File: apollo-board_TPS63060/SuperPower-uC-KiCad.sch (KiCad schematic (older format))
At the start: 5 parts, among them J10 Conn_01x13_Male

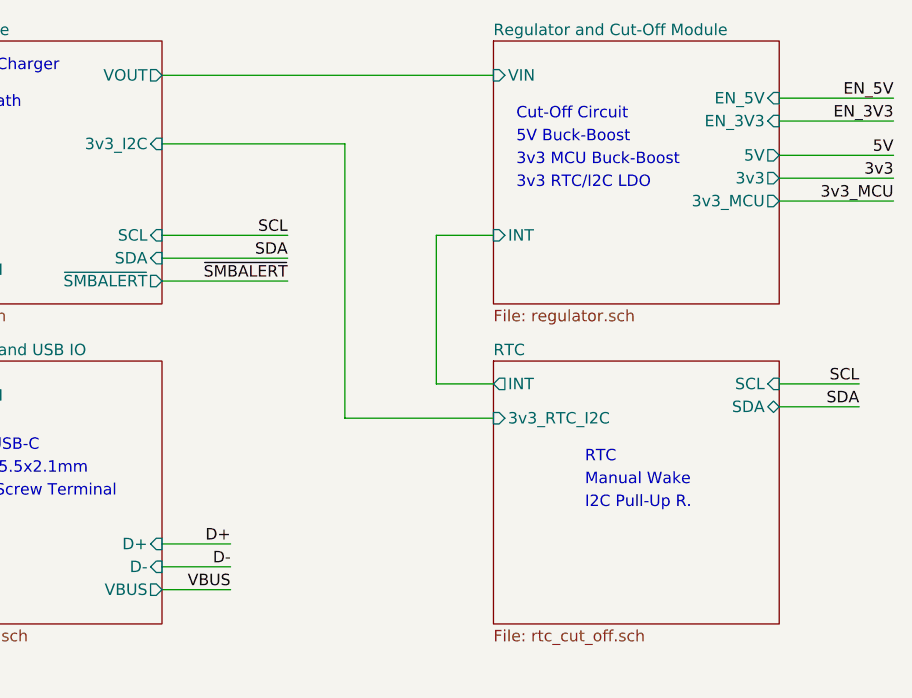
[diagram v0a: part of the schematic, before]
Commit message: Recreate TPS709 symbol to and set footprint to SOT23-5
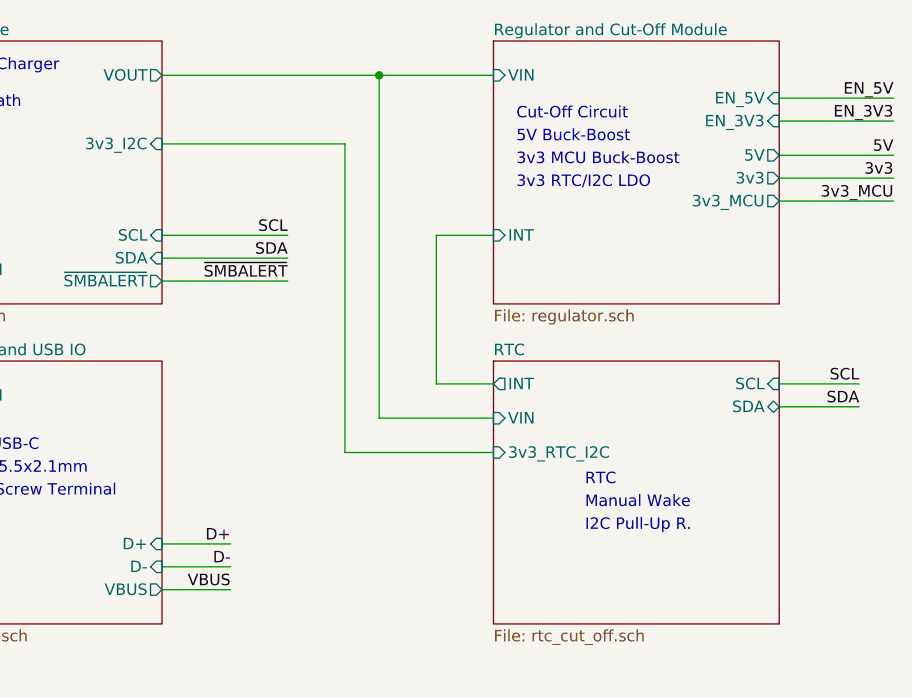
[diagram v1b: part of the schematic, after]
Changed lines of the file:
@@
 Text Notes 5850 2550 0    50   ~ 0
 5V Buck-Boost
-Text Notes 6150 3950 0    50   ~ 0
+Text Notes 6150 4050 0    50   ~ 0
 RTC
 Text Notes 5850 2450 0    50   ~ 0
@@
 Text Notes 3100 4100 0    50   ~ 0
 Solder Pads / Screw Terminal
-Text Notes 6150 4050 0    50   ~ 0
+Text Notes 6150 4150 0    50   ~ 0
 Manual Wake
 $Sheet
@@
 F2 "SCL" I R 7000 3600 50
 F3 "SDA" B R 7000 3700 50
-F4 "3v3_RTC_I2C" I L 5750 3750 50
+F4 "3v3_RTC_I2C" I L 5750 3900 50
 F5 "INT" O L 5750 3600 50
+F6 "VIN" I L 5750 3750 50
 $EndSheet
 Wire Wire Line
 	2950 3100 2950 3650
 Wire Wire Line
-	5750 2250 4300 2250
+	5750 2250 5250 2250
 Text Label 4850 2950 2    50   ~ 0
 SCL
@@
 F8 "INT" I L 5750 2950 50
 $EndSheet
-Text Notes 6150 4150 0    50   ~ 0
+Text Notes 6150 4250 0    50   ~ 0
 I2C Pull-Up R.
 Wire Wire Line
 	5100 2550 4300 2550
-Wire Wire Line
-	5750 3750 5100 3750
-Wire Wire Line
-	5100 2550 5100 3750
 Wire Wire Line
 	5500 3600 5500 2950
@@
 Wire Notes Line
 	1300 5350 2550 5350
+Wire Wire Line
+	5750 3900 5100 3900
+Wire Wire Line
+	5100 2550 5100 3900
+Wire Wire Line
+	5750 3750 5250 3750
+Wire Wire Line
+	5250 3750 5250 2250
+Connection ~ 5250 2250
+Wire Wire Line
+	5250 2250 4300 2250
 $EndSCHEMATC

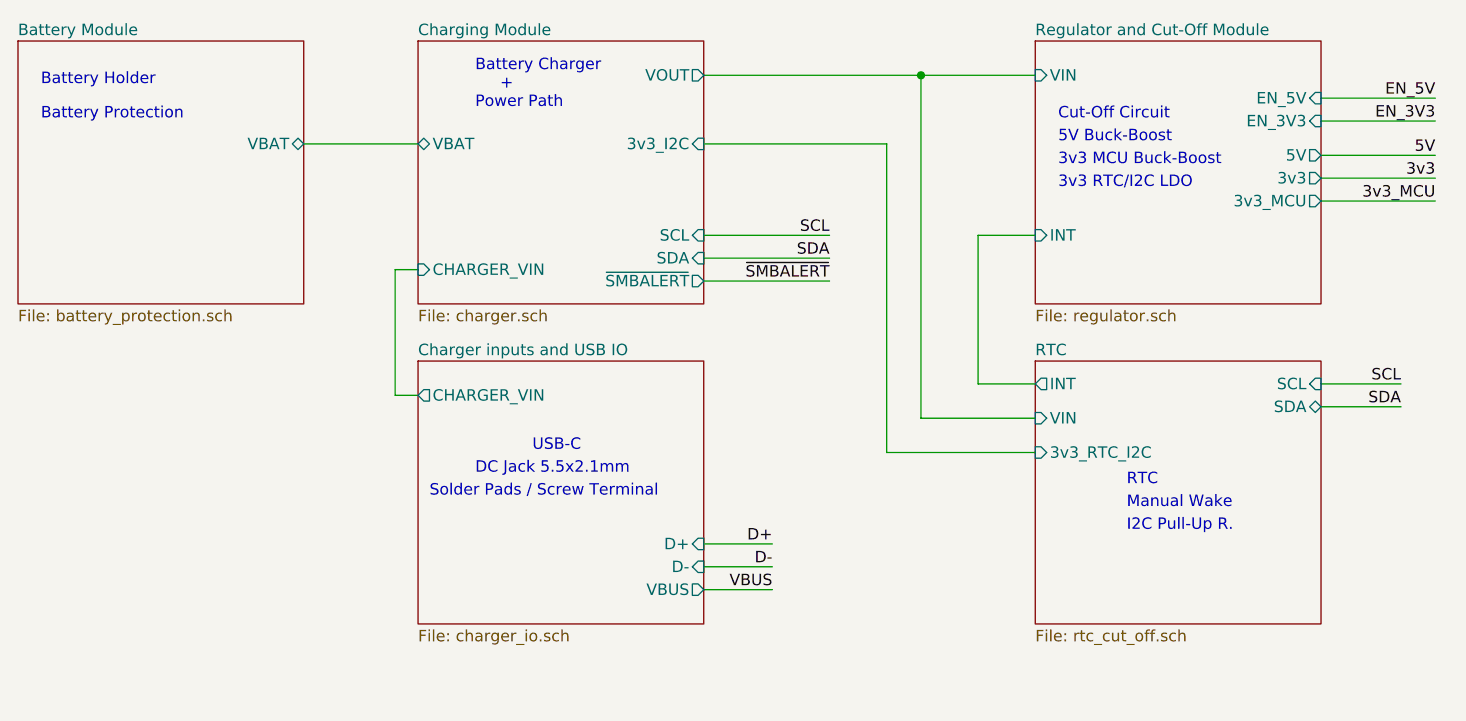
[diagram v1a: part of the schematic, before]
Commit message: Update "Main Schematic" text
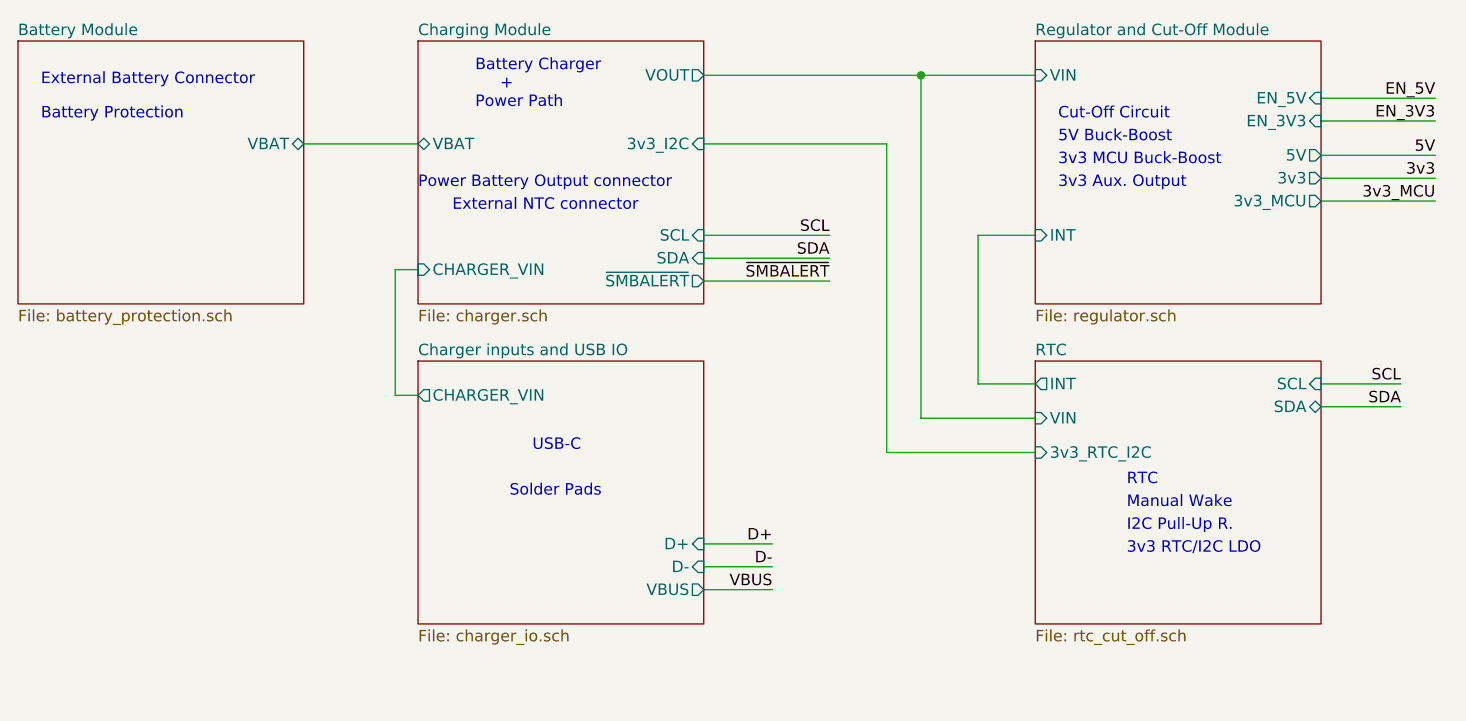
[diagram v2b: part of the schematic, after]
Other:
- note added: "3v3 Aux. Output"
- note added: "External Battery Connector"
- note added: "External NTC connector"
- note added: "Power Battery Output connector"
- note added: "Solder Pads"
- note removed: "Battery Holder"
- note removed: "DC Jack 5.5x2.1mm"
- note removed: "Solder Pads / Screw Terminal"
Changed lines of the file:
@@
 	2550 2550 3050 2550
 Text Notes 1400 2300 0    50   ~ 0
-Battery Holder
+External Battery Connector
 Text Notes 1400 2450 0    50   ~ 0
 Battery Protection
 Text Notes 3300 2400 0    50   ~ 0
 Battery Charger\n     +\nPower Path
-Text Notes 5850 2750 0    50   ~ 0
+Text Notes 6150 4350 0    50   ~ 0
 3v3 RTC/I2C LDO
 Text Notes 5850 2650 0    50   ~ 0
@@
 Text Notes 3550 3900 0    50   ~ 0
 USB-C
-Text Notes 3300 4000 0    50   ~ 0
-DC Jack 5.5x2.1mm
-Text Notes 3100 4100 0    50   ~ 0
-Solder Pads / Screw Terminal
+Text Notes 3450 4100 0    50   ~ 0
+Solder Pads
 Text Notes 6150 4150 0    50   ~ 0
 Manual Wake
@@
 Wire Wire Line
 	5250 2250 4300 2250
+Text Notes 3050 2750 0    50   ~ 0
+Power Battery Output connector
+Text Notes 3200 2850 0    50   ~ 0
+External NTC connector
+Text Notes 5850 2750 0    50   ~ 0
+3v3 Aux. Output
 $EndSCHEMATC

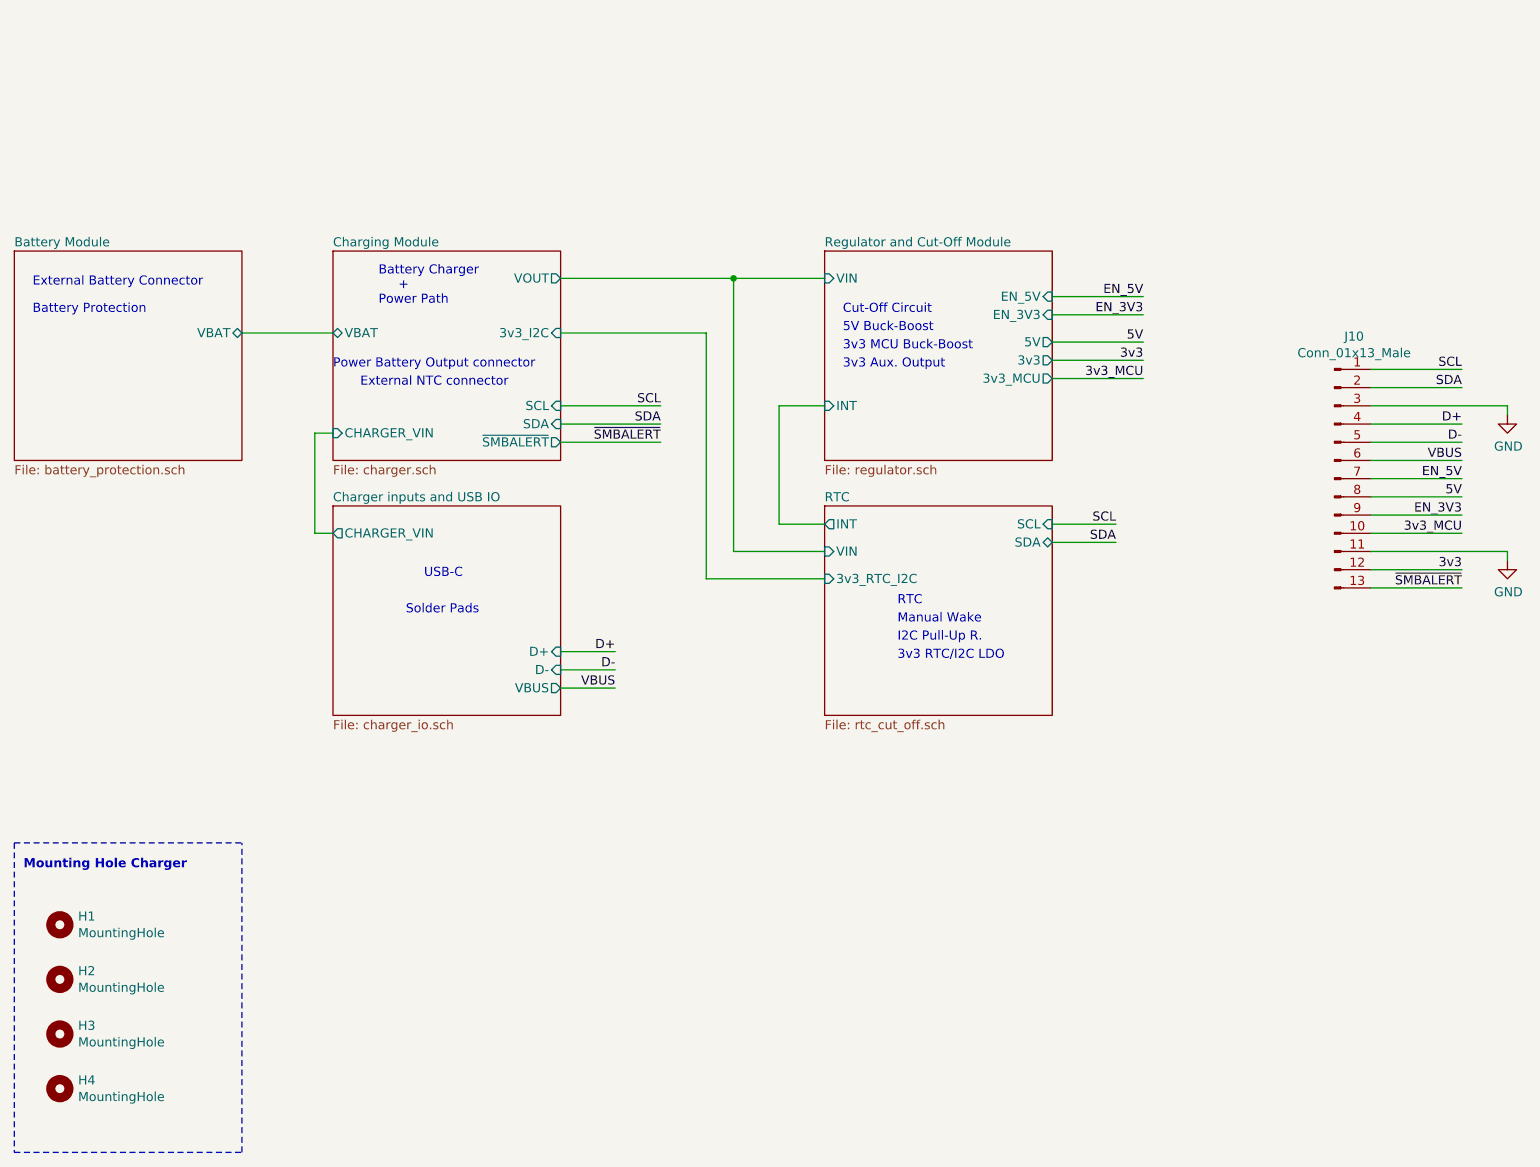
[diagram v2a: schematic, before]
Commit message: Rename some power signal on Schematic to improve readability.
+ Misc. updates
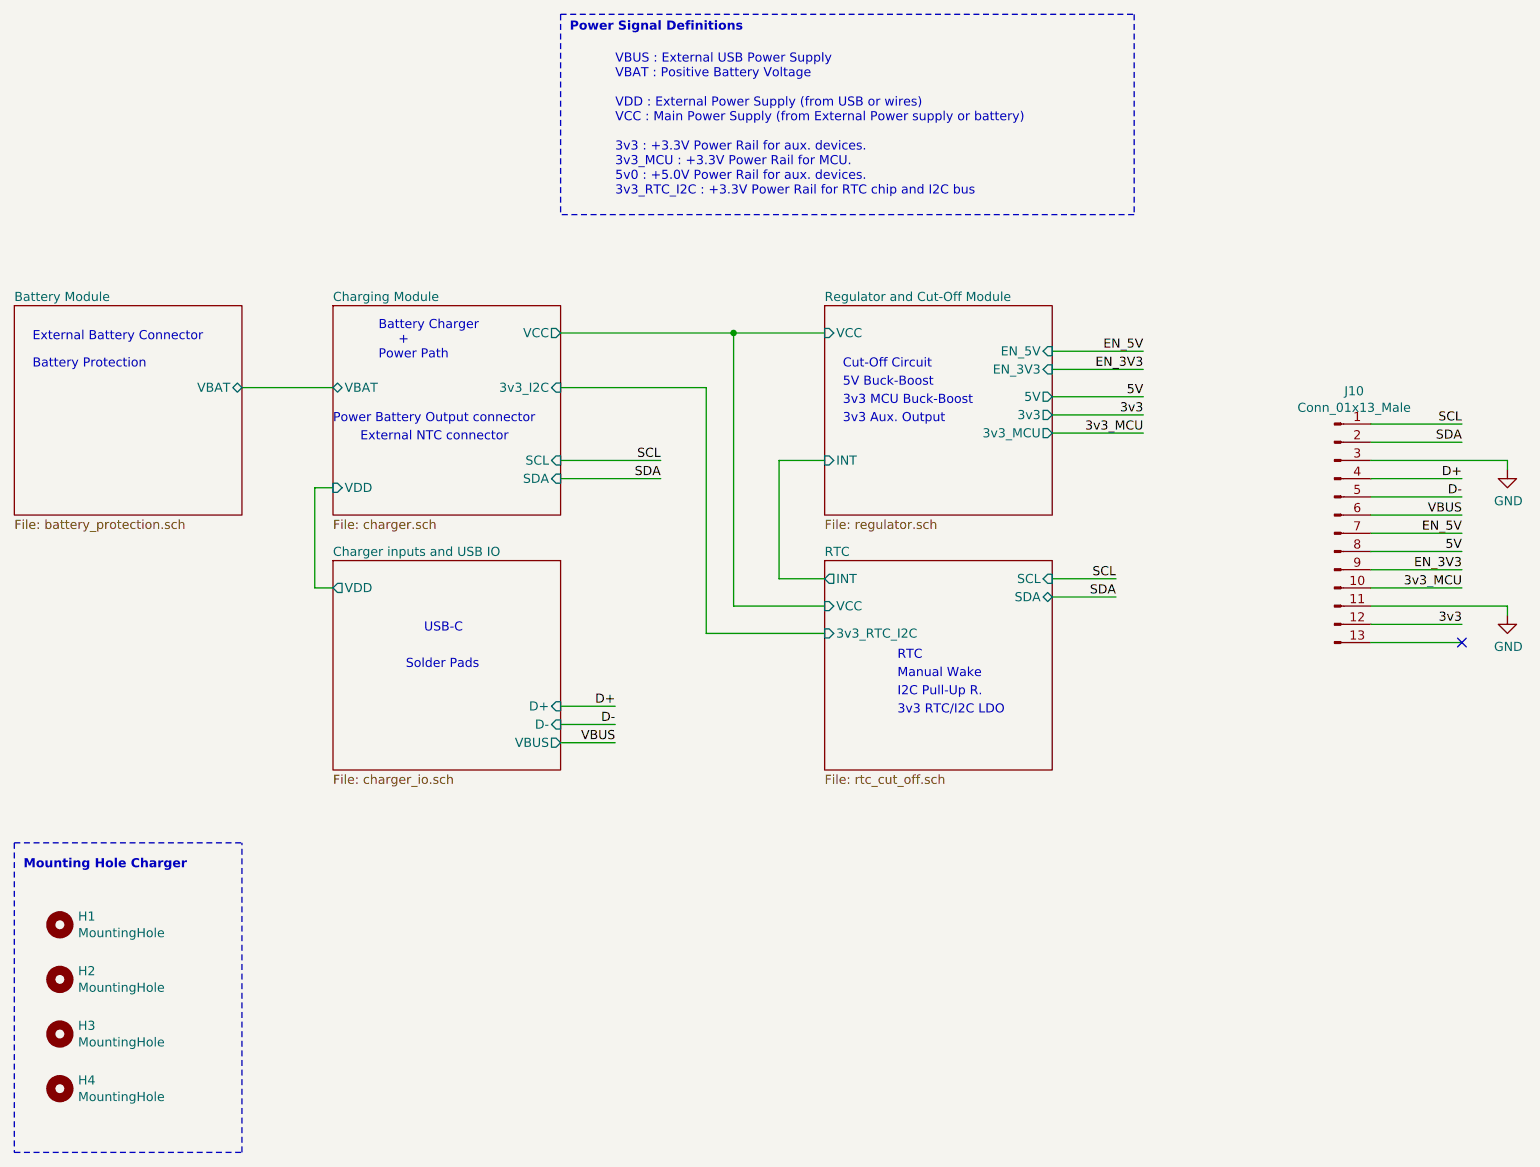
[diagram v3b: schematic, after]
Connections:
- net ~SMBALERT: no longer names the net of J10.13 (Pin_13)
- no-connect marks 0 -> 1
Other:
- note added: "Power Signal Definitions"
- note added: "VBUS : External USB Power Supply\nVBAT : Positive Battery Voltage\n\nVDD : External Power Supply (from USB or wires)\nVCC : Main Power Supply (from External Power supply or battery)\n\n3v3 : +3.3V Power Rail for aux. devices.\n3v3_MCU : +3.3V Power Rail for MCU.\n5v0 : +5.0V Power Rail for aux. devices.\n3v3_RTC_I2C : +3.3V Power Rail for RTC chip and I2C bus"
- moved on the sheet: J10
